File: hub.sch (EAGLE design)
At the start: 54 parts, among them IC2 24C02CSN, U1 LM3526, X1 12MHz

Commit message: BOM fix: swap 0603 18pF caps for 0805
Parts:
- C14, C15: DIGIKEY 1276-1089-1-ND -> 1276-1107-1-ND; MPN CL10C180JB8NNNC -> CL21C180JBANNNC; OC_MOUSER 77-VJ0603A180JXACBC -> 77-VJ0805A180GXACBC
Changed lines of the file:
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@@
 <part name="SUPPLY4" library="supply2" library_urn="urn:adsk.eagle:library:372" deviceset="GND" device=""/>
 <part name="C14" library="rcl" deviceset="C-EU" device="C0805" package3d_urn="urn:adsk.eagle:package:23617/2" value="18pF">
-<attribute name="DIGIKEY" value="1276-1089-1-ND"/>
-<attribute name="MPN" value="CL10C180JB8NNNC"/>
-<attribute name="OC_MOUSER" value="77-VJ0603A180JXACBC"/>
+<attribute name="DIGIKEY" value="1276-1107-1-ND"/>
+<attribute name="MPN" value="CL21C180JBANNNC"/>
+<attribute name="OC_MOUSER" value="77-VJ0805A180GXACBC"/>
 </part>
 <part name="C15" library="rcl" deviceset="C-EU" device="C0805" package3d_urn="urn:adsk.eagle:package:23617/2" value="18pF">
-<attribute name="DIGIKEY" value="1276-1089-1-ND"/>
-<attribute name="MPN" value="CL10C180JB8NNNC"/>
-<attribute name="OC_MOUSER" value="77-VJ0603A180JXACBC"/>
+<attribute name="DIGIKEY" value="1276-1107-1-ND"/>
+<attribute name="MPN" value="CL21C180JBANNNC"/>
+<attribute name="OC_MOUSER" value="77-VJ0805A180GXACBC"/>
 </part>
 <part name="SUPPLY5" library="supply2" library_urn="urn:adsk.eagle:library:372" deviceset="GND" device=""/>

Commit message: BOM fix: swap 0603 649R for 0805
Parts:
- R3: DIGIKEY P649HCT-ND -> 311-649CRCT-ND; MPN ERJ-6ENF6490V -> RC0805FR-07649RL; OC_MOUSER 667-ERJ-6ENF6490V -> 603-RC0805FR-07649RL
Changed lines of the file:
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@@
 <part name="SUPPLY3" library="supply2" library_urn="urn:adsk.eagle:library:372" deviceset="GND" device=""/>
 <part name="R3" library="rcl" deviceset="R-US_" device="M0805" package3d_urn="urn:adsk.eagle:package:23556/1" value="650R 1%">
-<attribute name="DIGIKEY" value="P649HCT-ND"/>
-<attribute name="MPN" value="ERJ-6ENF6490V"/>
-<attribute name="OC_MOUSER" value="667-ERJ-6ENF6490V"/>
+<attribute name="DIGIKEY" value="311-649CRCT-ND"/>
+<attribute name="MPN" value="RC0805FR-07649RL"/>
+<attribute name="OC_MOUSER" value="603-RC0805FR-07649RL"/>
 </part>
 <part name="SUPPLY4" library="supply2" library_urn="urn:adsk.eagle:library:372" deviceset="GND" device=""/>

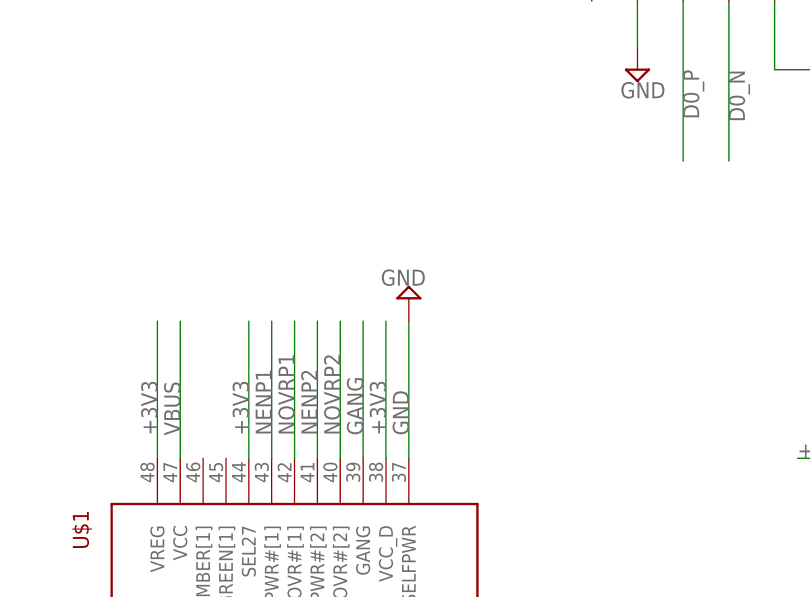
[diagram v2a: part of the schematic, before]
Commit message: pin-strap SELFPWR to +3V3 (bus-powered → self-powered)
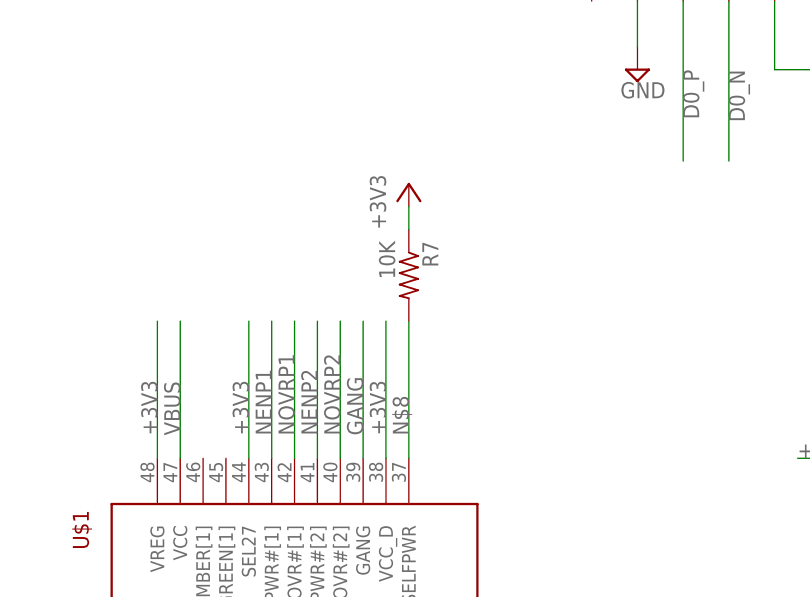
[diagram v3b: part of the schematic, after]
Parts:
- added R7: 10K, rcl:R-US_M0805
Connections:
- new net N$8: R7.2, U$1.SELFPWR
- net +3V3: now also R7.1
- net GND: no longer U$1.SELFPWR
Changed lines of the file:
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@@
 <grid distance="0.1" unitdist="inch" unit="inch" style="lines" multiple="1" display="no" altdistance="0.01" altunitdist="inch" altunit="inch"/>
 <layers>
-<layer number="1" name="Top" color="4" fill="1" visible="yes" active="no"/>
-<layer number="2" name="Route2" color="10" fill="1" visible="yes" active="no"/>
-<layer number="15" name="Route15" color="14" fill="1" visible="yes" active="no"/>
-<layer number="16" name="Bottom" color="1" fill="1" visible="yes" active="no"/>
-<layer number="17" name="Pads" color="2" fill="1" visible="yes" active="no"/>
-<layer number="18" name="Vias" color="2" fill="1" visible="yes" active="no"/>
-<layer number="19" name="Unrouted" color="6" fill="1" visible="yes" active="no"/>
-<layer number="20" name="Dimension" color="24" fill="1" visible="yes" active="no"/>
-<layer number="21" name="tPlace" color="7" fill="1" visible="yes" active="no"/>
-<layer number="22" name="bPlace" color="7" fill="1" visible="yes" active="no"/>
-<layer number="23" name="tOrigins" color="15" fill="1" visible="yes" active="no"/>
-<layer number="24" name="bOrigins" color="15" fill="1" visible="yes" active="no"/>
-<layer number="25" name="tNames" color="7" fill="1" visible="yes" active="no"/>
-<layer number="26" name="bNames" color="7" fill="1" visible="yes" active="no"/>
-<layer number="27" name="tValues" color="7" fill="1" visible="yes" active="no"/>
-<layer number="28" name="bValues" color="7" fill="1" visible="yes" active="no"/>
+<layer number="1" name="Top" color="4" fill="1" visible="no" active="no"/>
+<layer number="2" name="Route2" color="10" fill="1" visible="no" active="no"/>
+<layer number="15" name="Route15" color="14" fill="1" visible="no" active="no"/>
+<layer number="16" name="Bottom" color="1" fill="1" visible="no" active="no"/>
+<layer number="17" name="Pads" color="2" fill="1" visible="no" active="no"/>
+<layer number="18" name="Vias" color="2" fill="1" visible="no" active="no"/>
+<layer number="19" name="Unrouted" color="6" fill="1" visible="no" active="no"/>
+<layer number="20" name="Dimension" color="24" fill="1" visible="no" active="no"/>
+<layer number="21" name="tPlace" color="7" fill="1" visible="no" active="no"/>
+<layer number="22" name="bPlace" color="7" fill="1" visible="no" active="no"/>
+<layer number="23" name="tOrigins" color="15" fill="1" visible="no" active="no"/>
+<layer number="24" name="bOrigins" color="15" fill="1" visible="no" active="no"/>
+<layer number="25" name="tNames" color="7" fill="1" visible="no" active="no"/>
+<layer number="26" name="bNames" color="7" fill="1" visible="no" active="no"/>
+<layer number="27" name="tValues" color="7" fill="1" visible="no" active="no"/>
+<layer number="28" name="bValues" color="7" fill="1" visible="no" active="no"/>
 <layer number="29" name="tStop" color="7" fill="3" visible="no" active="no"/>
 <layer number="30" name="bStop" color="7" fill="6" visible="no" active="no"/>
@@
 <layer number="35" name="tGlue" color="7" fill="4" visible="no" active="no"/>
 <layer number="36" name="bGlue" color="7" fill="5" visible="no" active="no"/>
-<layer number="37" name="tTest" color="7" fill="1" visible="yes" active="no"/>
-<layer number="38" name="bTest" color="7" fill="1" visible="yes" active="no"/>
+<layer number="37" name="tTest" color="7" fill="1" visible="no" active="no"/>
+<layer number="38" name="bTest" color="7" fill="1" visible="no" active="no"/>
 <layer number="39" name="tKeepout" color="4" fill="11" visible="no" active="no"/>
 <layer number="40" name="bKeepout" color="1" fill="11" visible="no" active="no"/>
@@
 <layer number="44" name="Drills" color="7" fill="1" visible="no" active="no"/>
 <layer number="45" name="Holes" color="7" fill="1" visible="no" active="no"/>
-<layer number="46" name="Milling" color="3" fill="1" visible="yes" active="no"/>
-<layer number="47" name="Measures" color="7" fill="1" visible="yes" active="no"/>
-<layer number="48" name="Document" color="7" fill="1" visible="yes" active="no"/>
-<layer number="49" name="Reference" color="7" fill="1" visible="yes" active="no"/>
-<layer number="50" name="dxf" color="7" fill="1" visible="yes" active="no"/>
-<layer number="51" name="tDocu" color="7" fill="1" visible="yes" active="no"/>
-<layer number="52" name="bDocu" color="7" fill="1" visible="yes" active="no"/>
-<layer number="53" name="tGND_GNDA" color="7" fill="9" visible="yes" active="no"/>
-<layer number="54" name="bGND_GNDA" color="1" fill="9" visible="yes" active="no"/>
-<layer number="56" name="wert" color="7" fill="1" visible="yes" active="no"/>
-<layer number="57" name="tCAD" color="7" fill="1" visible="yes" active="no"/>
-<layer number="59" name="tCarbon" color="7" fill="1" visible="yes" active="no"/>
-<layer number="60" name="bCarbon" color="7" fill="1" visible="yes" active="no"/>
+<layer number="46" name="Milling" color="3" fill="1" visible="no" active="no"/>
+<layer number="47" name="Measures" color="7" fill="1" visible="no" active="no"/>
+<layer number="48" name="Document" color="7" fill="1" visible="no" active="no"/>
+<layer number="49" name="Reference" color="7" fill="1" visible="no" active="no"/>
+<layer number="50" name="dxf" color="7" fill="1" visible="no" active="no"/>
+<layer number="51" name="tDocu" color="7" fill="1" visible="no" active="no"/>
+<layer number="52" name="bDocu" color="7" fill="1" visible="no" active="no"/>
+<layer number="53" name="tGND_GNDA" color="7" fill="9" visible="no" active="no"/>
+<layer number="54" name="bGND_GNDA" color="1" fill="9" visible="no" active="no"/>
+<layer number="56" name="wert" color="7" fill="1" visible="no" active="no"/>
+<layer number="57" name="tCAD" color="7" fill="1" visible="no" active="no"/>
+<layer number="59" name="tCarbon" color="7" fill="1" visible="no" active="no"/>
+<layer number="60" name="bCarbon" color="7" fill="1" visible="no" active="no"/>
 <layer number="88" name="SimResults" color="9" fill="1" visible="yes" active="yes"/>
 <layer number="89" name="SimProbes" color="9" fill="1" visible="yes" active="yes"/>
@@
 <attribute name="OC_MOUSER" value="81-GRM40X104K50L"/>
 </part>
-<part name="SUPPLY25" library="supply2" library_urn="urn:adsk.eagle:library:372" deviceset="GND" device=""/>
 <part name="P+1" library="supply1" library_urn="urn:adsk.eagle:library:371" deviceset="V+" device=""/>
 <part name="P+2" library="supply1" library_urn="urn:adsk.eagle:library:371" deviceset="V+" device=""/>
@@
 </part>
 <part name="SUPPLY26" library="supply2" library_urn="urn:adsk.eagle:library:372" deviceset="GND" device=""/>
+<part name="R7" library="rcl" deviceset="R-US_" device="M0805" package3d_urn="urn:adsk.eagle:package:23556/1" value="10K">
+<attribute name="DIGIKEY" value="311-10.0KCRCT-ND"/>
+<attribute name="MPN" value="RC0805FR-0710KL"/>
+<attribute name="OC_MOUSER" value="603-RC0805FR-0710KL"/>
+</part>
+<part name="+3V3_7" library="supply1" library_urn="urn:adsk.eagle:library:371" deviceset="+3V3" device=""/>
 </parts>
 <sheets>
@@
 <attribute name="DIGIKEY" x="193.04" y="71.12" size="1.778" layer="96" display="off"/>
 </instance>
-<instance part="SUPPLY25" gate="GND" x="12.7" y="48.26" rot="R180"/>
 <instance part="P+1" gate="1" x="86.36" y="48.26"/>
 <instance part="P+2" gate="1" x="114.3" y="48.26"/>
@@
 </instance>
 <instance part="SUPPLY26" gate="GND" x="200.66" y="-91.44" rot="R90"/>
+<instance part="R7" gate="G$1" x="12.7" y="50.8" rot="R270">
+<attribute name="DIGIKEY" x="12.7" y="50.8" size="1.778" layer="96" rot="R270" display="off"/>
+<attribute name="MPN" x="12.7" y="50.8" size="1.778" layer="96" rot="R270" display="off"/>
+<attribute name="OC_MOUSER" x="12.7" y="50.8" size="1.778" layer="96" rot="R270" display="off"/>
+</instance>
+<instance part="+3V3_7" gate="G$1" x="12.7" y="60.96"/>
 </instances>
 <busses>
@@
 <junction x="48.26" y="-93.98"/>
 <pinref part="SUPPLY20" gate="GND" pin="GND"/>
-</segment>
-<segment>
-<pinref part="U$1" gate="G$1" pin="SELFPWR"/>
-<wire x1="12.7" y1="30.48" x2="12.7" y2="45.72" width="0.1524" layer="91"/>
-<label x="12.7" y="33.02" size="1.778" layer="95" rot="R90"/>
-<pinref part="SUPPLY25" gate="GND" pin="GND"/>
 </segment>
 <segment>
@@
 <wire x1="182.88" y1="-91.44" x2="182.88" y2="-93.98" width="0.1524" layer="91"/>
 <junction x="182.88" y="-91.44"/>
+</segment>
+<segment>
+<pinref part="R7" gate="G$1" pin="1"/>
+<pinref part="+3V3_7" gate="G$1" pin="+3V3"/>
+<wire x1="12.7" y1="55.88" x2="12.7" y2="58.42" width="0.1524" layer="91"/>
 </segment>
 </net>
@@
 </segment>
 </net>
+<net name="N$8" class="0">
+<segment>
+<pinref part="U$1" gate="G$1" pin="SELFPWR"/>
+<wire x1="12.7" y1="30.48" x2="12.7" y2="45.72" width="0.1524" layer="91"/>
+<label x="12.7" y="33.02" size="1.778" layer="95" rot="R90"/>
+<pinref part="R7" gate="G$1" pin="2"/>
+</segment>
+</net>

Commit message: Change 0.1μF capacitors from 490-1666-1-ND to 732-8026-1-ND
The former is no longer available.
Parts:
- C1, C10, C11, C12, C16, C17, C19, C20, C21, C22, C4, C6, C8, C9: DIGIKEY 490-1666-1-ND -> 732-8026-1-ND
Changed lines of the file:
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@@
 <part name="SUPPLY7" library="supply2" library_urn="urn:adsk.eagle:library:372" deviceset="GND" device=""/>
 <part name="C19" library="rcl" deviceset="C-EU" device="C0805" package3d_urn="urn:adsk.eagle:package:23617/2" value="0.1uF">
-<attribute name="DIGIKEY" value="490-1666-1-ND"/>
+<attribute name="DIGIKEY" value="732-8026-1-ND"/>
 <attribute name="MPN" value="GRM21BR71H104KA01L"/>
 <attribute name="OC_MOUSER" value="81-GRM40X104K50L"/>
@@
 </part>
 <part name="C16" library="rcl" deviceset="C-EU" device="C0805" package3d_urn="urn:adsk.eagle:package:23617/2" value="0.1uF">
-<attribute name="DIGIKEY" value="490-1666-1-ND"/>
+<attribute name="DIGIKEY" value="732-8026-1-ND"/>
 <attribute name="MPN" value="GRM21BR71H104KA01L"/>
 <attribute name="OC_MOUSER" value="81-GRM40X104K50L"/>
@@
 <part name="SUPPLY13" library="supply2" library_urn="urn:adsk.eagle:library:372" deviceset="GND" device=""/>
 <part name="C20" library="rcl" deviceset="C-EU" device="C0805" package3d_urn="urn:adsk.eagle:package:23617/2" value="0.1uF">
-<attribute name="DIGIKEY" value="490-1666-1-ND"/>
+<attribute name="DIGIKEY" value="732-8026-1-ND"/>
 <attribute name="MPN" value="GRM21BR71H104KA01L"/>
 <attribute name="OC_MOUSER" value="81-GRM40X104K50L"/>
@@
 <part name="SUPPLY16" library="supply2" library_urn="urn:adsk.eagle:library:372" deviceset="GND" device=""/>
 <part name="C1" library="rcl" deviceset="C-EU" device="C0805" package3d_urn="urn:adsk.eagle:package:23617/2" value="0.1uF">
-<attribute name="DIGIKEY" value="490-1666-1-ND"/>
+<attribute name="DIGIKEY" value="732-8026-1-ND"/>
 <attribute name="MPN" value="GRM21BR71H104KA01L"/>
 <attribute name="OC_MOUSER" value="81-GRM40X104K50L"/>
@@
 </part>
 <part name="C4" library="rcl" deviceset="C-EU" device="C0805" package3d_urn="urn:adsk.eagle:package:23617/2" value="0.1uF">
-<attribute name="DIGIKEY" value="490-1666-1-ND"/>
+<attribute name="DIGIKEY" value="732-8026-1-ND"/>
 <attribute name="MPN" value="GRM21BR71H104KA01L"/>
 <attribute name="OC_MOUSER" value="81-GRM40X104K50L"/>
@@
 </part>
 <part name="C8" library="rcl" deviceset="C-EU" device="C0805" package3d_urn="urn:adsk.eagle:package:23617/2" value="0.1uF">
-<attribute name="DIGIKEY" value="490-1666-1-ND"/>
+<attribute name="DIGIKEY" value="732-8026-1-ND"/>
 <attribute name="MPN" value="GRM21BR71H104KA01L"/>
 <attribute name="OC_MOUSER" value="81-GRM40X104K50L"/>
@@
 <part name="SUPPLY18" library="supply2" library_urn="urn:adsk.eagle:library:372" deviceset="GND" device=""/>
 <part name="C9" library="rcl" deviceset="C-EU" device="C0805" package3d_urn="urn:adsk.eagle:package:23617/2" value="0.1uF">
-<attribute name="DIGIKEY" value="490-1666-1-ND"/>
+<attribute name="DIGIKEY" value="732-8026-1-ND"/>
 <attribute name="MPN" value="GRM21BR71H104KA01L"/>
 <attribute name="OC_MOUSER" value="81-GRM40X104K50L"/>
 </part>
 <part name="C10" library="rcl" deviceset="C-EU" device="C0805" package3d_urn="urn:adsk.eagle:package:23617/2" value="0.1uF">
-<attribute name="DIGIKEY" value="490-1666-1-ND"/>
+<attribute name="DIGIKEY" value="732-8026-1-ND"/>
 <attribute name="MPN" value="GRM21BR71H104KA01L"/>
 <attribute name="OC_MOUSER" value="81-GRM40X104K50L"/>
 </part>
 <part name="C11" library="rcl" deviceset="C-EU" device="C0805" package3d_urn="urn:adsk.eagle:package:23617/2" value="0.1uF">
-<attribute name="DIGIKEY" value="490-1666-1-ND"/>
+<attribute name="DIGIKEY" value="732-8026-1-ND"/>
 <attribute name="MPN" value="GRM21BR71H104KA01L"/>
 <attribute name="OC_MOUSER" value="81-GRM40X104K50L"/>
@@
 </part>
 <part name="C17" library="rcl" deviceset="C-EU" device="C0805" package3d_urn="urn:adsk.eagle:package:23617/2" value="0.1uF">
-<attribute name="DIGIKEY" value="490-1666-1-ND"/>
+<attribute name="DIGIKEY" value="732-8026-1-ND"/>
 <attribute name="MPN" value="GRM21BR71H104KA01L"/>
 <attribute name="OC_MOUSER" value="81-GRM40X104K50L"/>
@@
 <part name="+3V3_4" library="supply1" library_urn="urn:adsk.eagle:library:371" deviceset="+3V3" device=""/>
 <part name="C12" library="rcl" deviceset="C-EU" device="C0805" package3d_urn="urn:adsk.eagle:package:23617/2" value="0.1uF">
-<attribute name="DIGIKEY" value="490-1666-1-ND"/>
+<attribute name="DIGIKEY" value="732-8026-1-ND"/>
 <attribute name="MPN" value="GRM21BR71H104KA01L"/>
 <attribute name="OC_MOUSER" value="81-GRM40X104K50L"/>
@@
 <part name="SUPPLY27" library="supply2" library_urn="urn:adsk.eagle:library:372" deviceset="GND" device=""/>
 <part name="C21" library="rcl" deviceset="C-EU" device="C0805" package3d_urn="urn:adsk.eagle:package:23617/2" value="0.1uF">
-<attribute name="DIGIKEY" value="490-1666-1-ND"/>
+<attribute name="DIGIKEY" value="732-8026-1-ND"/>
 <attribute name="MPN" value="GRM21BR71H104KA01L"/>
 <attribute name="OC_MOUSER" value="81-GRM40X104K50L"/>
@@
 <part name="SUPPLY31" library="supply2" library_urn="urn:adsk.eagle:library:372" deviceset="GND" device=""/>
 <part name="C22" library="rcl" deviceset="C-EU" device="C0805" package3d_urn="urn:adsk.eagle:package:23617/2" value="0.1uF">
-<attribute name="DIGIKEY" value="490-1666-1-ND"/>
+<attribute name="DIGIKEY" value="732-8026-1-ND"/>
 <attribute name="MPN" value="GRM21BR71H104KA01L"/>
 <attribute name="OC_MOUSER" value="81-GRM40X104K50L"/>
@@
 <part name="+3V3_6" library="supply1" library_urn="urn:adsk.eagle:library:371" deviceset="+3V3" device=""/>
 <part name="C6" library="rcl" deviceset="C-EU" device="C0805" package3d_urn="urn:adsk.eagle:package:23617/2" value="0.1uF">
-<attribute name="DIGIKEY" value="490-1666-1-ND"/>
-<attribute name="MPN" value="GRM21BR71H104KA01L"/>
-<attribute name="OC_MOUSER" value="81-GRM40X104K50L"/>
+<attribute name="DIGIKEY" value="732-8026-1-ND"/>
+<attribute name="MPN" value="GRM21BR71H104KA01L"/>
+<attribute name="OC_MOUSER" value="81-GRM40X104K50L"/>
